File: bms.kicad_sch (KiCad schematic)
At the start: 27 parts, among them J1 I2C+ALERT, Q1 30V/20A_NFET, Q2 30V/20A_NFET, U1 BQ7692003

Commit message: sourcing: lock LCSC + MPN + Manufacturer + Footprint for every remaining BOM line
Applied JLCPCB picks (LCSC number + manufacturer part number + tuned
footprint) across all four sub-sheets — 72 components total.  Every
placed component now carries LCSC, MPN, and Manufacturer properties;
the built-in Value/Footprint fields point to the exact JLCPCB stock
unit for that pick.

Highlights:
- ICs (Preferred where available, Extended otherwise):
    U1(bms)      BQ7692003PWR   C601650    TSSOP-20
    U1(charger)  IP2326         C2832094   VQFN-24 EP4x4
    U1(input)    CH224K         C970725    ESSOP-10
    U1(bckbst)   LM5176PWPR     C442493    HTSSOP-28
- Diodes + TVS (all Preferred tier):
    D1(input)    SRV05-4        C7420376   SOT-23-6   (622K stock)
    D2(input)    SMAJ12A        C19077531  SMA        ( 33K stock)
    D1-3(bms)    SMAJ15A        C19077535  SMA        (174K stock)
- Power passives:
    L1(bckbst)   6.8uH 5A       C167221    FXL0630-6R8-M  7x6.6mm
    L1(charger)  2.2uH 4.8A     C602029    FHD4020S-2R2MT 4x4mm
    FB1(input)   600R@100MHz    C139183    CBW160808U601T 0603 (1A)
    R9(bms)      5mR 2W ±1%     C185817    RLM25FEER005   2512
- Bulk passives — Uniohm 0603WAF series, ±1%, high stock.  All caps
  Samsung/Yageo 0603 or 0805 ceramic.  Reused Q1-Q4 = AON7544
  (already locked at 9120877) for bms.Q1/Q2 too — same part
  covers 30V/20A pack-return FET stack.

Effect on pre-fab readiness (kicad-happy):
- SS-001 error CLEARED — 1/34 MPN coverage was blocking pre-fab;
  now 34/34 (100%).
- DS-002 warning shifted: was "no datasheets" (2/34 MPNs), now
  "no datasheets dir" (34/34 MPNs).  Non-blocking; datasheet PDFs
  are nice-to-have but the review can proceed without them.
- 1 remaining error PP-001 (LM5176_VCC no DC source) is a false
  positive: KiCad library symbol declares VCC as power_in but it's
  actually the LM5176's internal 5V LDO OUTPUT.  Accepted as-is.

Full-project ERC still 0 errors.  Schematic is now sourcing-clean
and ready for 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
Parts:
- BAT1: value 3× 18650 -> BH-18650-B5BA016; LCSC (none) -> C19184086; MPN (none) -> BH-18650-B5BA016; Manufacturer (none) -> MYOUNG
- C1, C2, C3, C4, C6: LCSC (none) -> C14663; MPN (none) -> CC0603KRX7R9BB104; Manufacturer (none) -> YAGEO
- C5, C7: LCSC (none) -> C15849; MPN (none) -> CL10A105KB8NNNC; Manufacturer (none) -> SAMSUNG
- D1, D2, D3: LCSC (none) -> C19077535; MPN (none) -> SMAJ15A; Manufacturer (none) -> LRC
- J1: LCSC (none) -> C492404; MPN (none) -> PZ254V-11-05P; Manufacturer (none) -> XKB Connectivity
- Q1, Q2: value 30V/20A_NFET -> AON7544; footprint Package_TO_SOT_SMD:SOIC-8_3.9x4.9mm_P1.27mm -> power_module_lib:DFN-8_L3.3-W3.3-P0.65-BL-2; LCSC (none) -> C315567; MPN (none) -> AON7544; Manufacturer (none) -> Alpha & Omega Semi
- R1, R10, R11, R2, R3, R4: LCSC (none) -> C22775; MPN (none) -> 0603WAF1000T5E; Manufacturer (none) -> Uniohm
- R5, R6, R7, R8: LCSC (none) -> C25804; MPN (none) -> 0603WAF1002T5E; Manufacturer (none) -> Uniohm
- R9: LCSC (none) -> C185817; MPN (none) -> RLM25FEER005; Manufacturer (none) -> Uniohm
- TH1: LCSC (none) -> C2889048; MPN (none) -> CMFA 103F3435; Manufacturer (none) -> CHIP-TEK
- U1: value BQ7692003 -> BQ7692003PWR; LCSC (none) -> C601650; MPN (none) -> BQ7692003PWR; Manufacturer (none) -> Texas Instruments

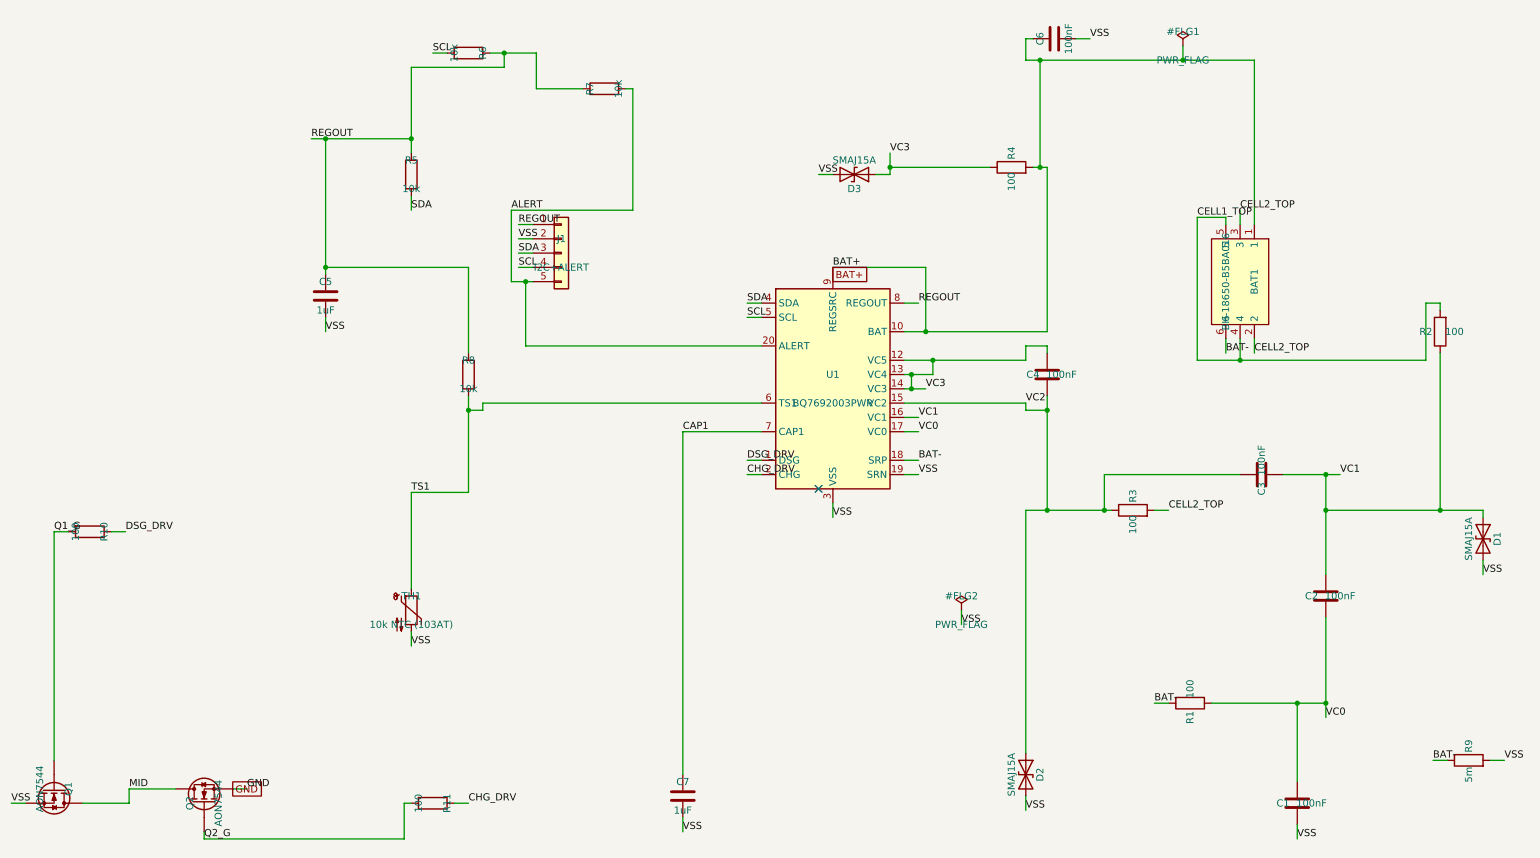
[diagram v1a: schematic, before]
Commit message: sheets: hierarchical ref disambiguation via annotate_schematic
Every sub-sheet symbol now carries a `_{SHEETNAME}{instance_num}` suffix so
refs are globally unique across the hierarchy.  76 refs rewritten:
  bms:       27 (e.g. U1 → U1_BMS1,      Q1 → Q1_BMS1)
  charger:   19 (e.g. U1 → U1_CHARGER1,  R7 → R7_CHARGER1)
  input:      8 (e.g. U1 → U1_INPUT1,    J1 → J1_INPUT1)
  buckboost: 22 (e.g. U1 → U1_BUCKBOOST1,Q1 → Q1_BUCKBOOST1)

Fixes kicad-cli's `schematic has annotation errors` warning which previously
caused BOM export to collapse the four different U1's (BQ76920 + IP2326 +
CH224K + LM5176) into a single row with comma-joined values.

bom_step1.csv committed alongside as the post-disambiguation baseline —
38 grouped rows, 100% LCSC/MPN coverage.

Applied via the new `annotate_schematic` hierarchical pass shipped in
KiCAD-MCP-Server c529efa on develop.  See NOTES.md for the mid-session
handoff block and memory `feedback_hierarchical_annotate`.

Co-Authored-By: Claude Opus 4.7 <noreply@anthropic.com>
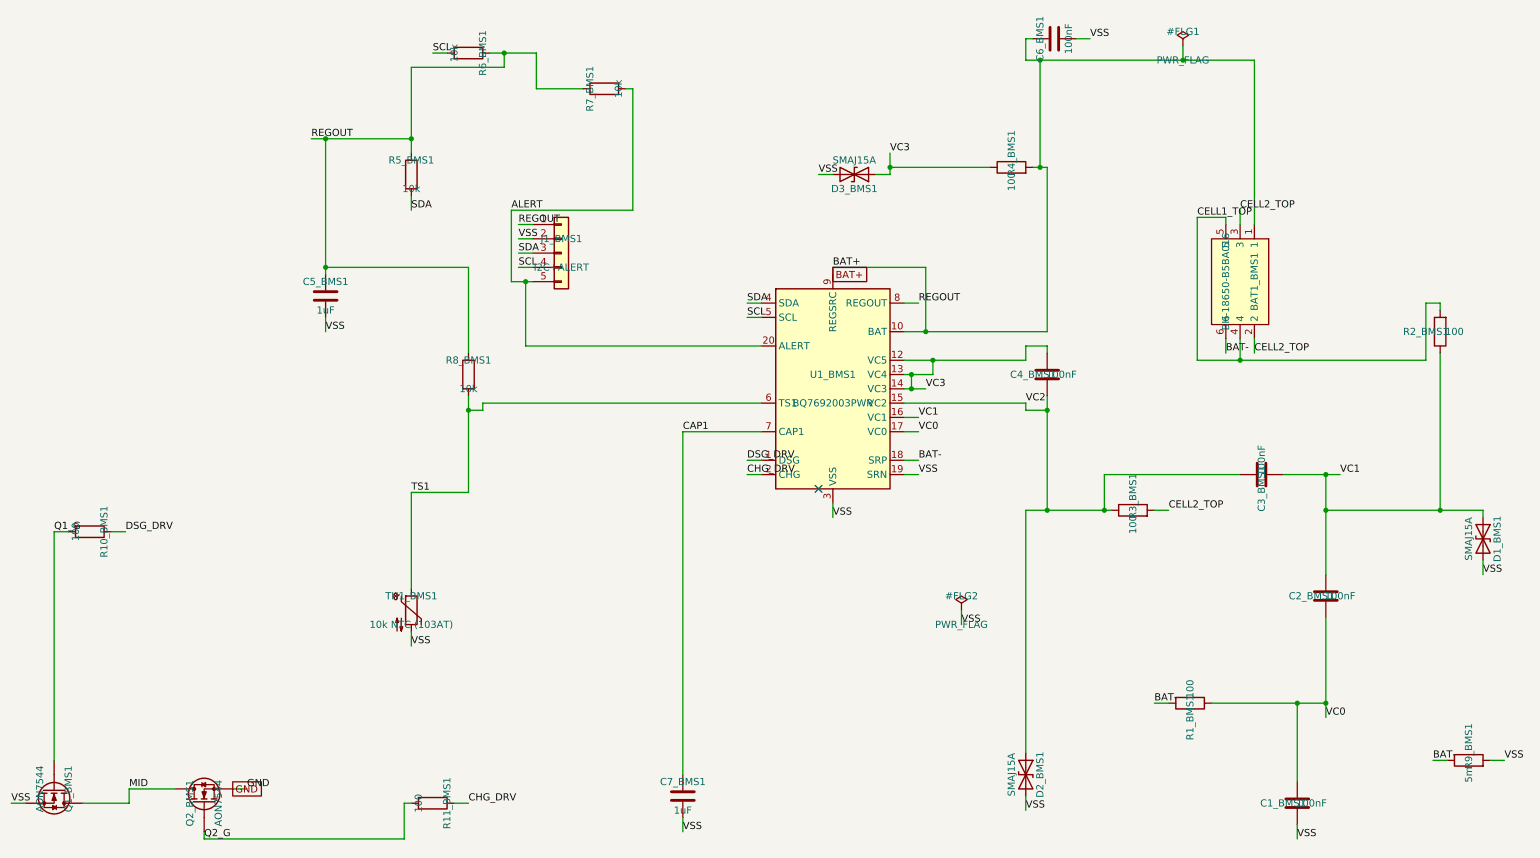
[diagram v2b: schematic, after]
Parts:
- renumbered BAT1 to BAT1_BMS1, C1 to C1_BMS1, C2 to C2_BMS1, C3 to C3_BMS1, C4 to C4_BMS1, C5 to C5_BMS1, C6 to C6_BMS1, C7 to C7_BMS1, D1 to D1_BMS1, D2 to D2_BMS1, D3 to D3_BMS1, J1 to J1_BMS1, Q1 to Q1_BMS1, Q2 to Q2_BMS1, R10 to R10_BMS1, R11 to R11_BMS1, R1 to R1_BMS1, R2 to R2_BMS1, R3 to R3_BMS1, R4 to R4_BMS1, R5 to R5_BMS1, R6 to R6_BMS1, R7 to R7_BMS1, R8 to R8_BMS1, R9 to R9_BMS1, TH1 to TH1_BMS1, U1 to U1_BMS1

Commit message: Step 2: complete Footprint set + sync 76 footprints to .kicad_pcb
Fill in the Footprint properties that were missing from the prior
sourcing pass, and sync everything to the PCB.

Footprint updates on the schematic:
- 35 passives got their Footprint assigned by value (0603 for R/C ≤1uF,
  0805 for 10uF/22uF caps).
- BAT1_BMS1 → power_module_lib:BAT-SMD_BH-18650-B5BA016 (was truncated).
- L1_BUCKBOOST1 → Inductor_SMD:L_Sumida_CDMC6D28_7.25x6.5mm (needed the
  size suffix so KiCad can resolve the .kicad_mod file).

Sync result: 76/76 footprints imported, 60 nets added, 245 pads assigned,
0 import errors.  Unmatched pads reported are all intentional NCs per
REQUIREMENTS.md (USB-C D+/D-, CH224K SBU/CFG, SRV05-4 unused ESD channels).

The footprints are at the default y=-140..-20 auto-import grid; no
placement work yet.  Next step is add_board_outline + set_design_rules.

For discoverability going forward, the pre-sync gap gets caught by
check_sourcing_readiness (KiCAD-MCP-Server fa93ba9 on develop) rather
than having to reset the .kicad_pcb after every retro-fill of an empty
Footprint property.

Co-Authored-By: Claude Opus 4.7 <noreply@anthropic.com>
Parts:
- BAT1_BMS1: footprint (none) -> power_module_lib:BAT-SMD_BH-18650-B5BA016

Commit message: Step 3+4 WIP: board outline, 4-layer stackup, decoupling spring classes, initial placement pass
Step 3 (board mechanics)
- Edge.Cuts rectangle 100x70 mm (BAT1 alone is 82.3x56.8 so 60x80 in
  the pre-session NOTES was too small)
- 4-layer stackup: added In1.Cu (GND plane) + In2.Cu (PWR plane)
- Design rules tightened: clearance 0.15, minTrackWidth 0.15,
  minViaDiameter 0.45, viaDrill 0.3

Step 4 (WIP — placement)
- 13 Pin_Spring_Class:{pad} = {"IC.pin": "DECOUPLING"} assignments on
  bypass caps across bms/charger/buckboost.  Every IC's power/reservoir/
  bootstrap cap now has an explicit DECOUPLING target so the auto-placer
  parks it right next to the IC pin instead of drifting off with the
  power-rail centroid:
    C7_BMS1        -> BQ76920 CAP1 (pin 7, charge pump reservoir)
    C5_BMS1        -> BQ76920 REGOUT bypass (pin 8)
    C6_BMS1        -> BQ76920 BAT+ sense
    C1..C4_BMS1    -> BQ76920 VCn sense RC filters
    C3_BUCKBOOST1  -> LM5176 BIAS bypass (pin 24, 2.2uF)
    C4_BUCKBOOST1  -> LM5176 VCC LDO bypass (pin 23, 1uF)
    C5_BUCKBOOST1  -> LM5176 BOOT1 bootstrap (pin 26)
    C6_BUCKBOOST1  -> LM5176 BOOT2 bootstrap (pin 20)
    C7_BUCKBOOST1  -> LM5176 SS (pin 8)
    C5_CHARGER1    -> IP2326 BST_CAP (pin 14)
- Initial relax_placement pass with 7 locked anchors (2 headers + BAT1 +
  4 ICs).  Not a shippable layout yet: USB-C is backwards, I2C header
  overlaps BAT1's B.Cu pad zone, Q1..Q4 + L1 (buck-boost power stage)
  scattered from LM5176.  Left as a starting point for hand-refinement.
- TH1_BMS1 (pack thermistor) flipped to B.Cu for proximity to the
  cells — final position to be set by hand.

Co-Authored-By: Claude Opus 4.7 <noreply@anthropic.com>
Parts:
- C1_BMS1: Pin_Spring_Class:2 (none) -> {"U1_BMS1.17":"DECOUPLING"}
- C2_BMS1: Pin_Spring_Class:2 (none) -> {"U1_BMS1.16":"DECOUPLING"}
- C3_BMS1: Pin_Spring_Class:2 (none) -> {"U1_BMS1.15":"DECOUPLING"}
- C4_BMS1: Pin_Spring_Class:2 (none) -> {"U1_BMS1.14":"DECOUPLING"}
- C5_BMS1: Pin_Spring_Class:1 (none) -> {"U1_BMS1.8":"DECOUPLING"}
- C6_BMS1: Pin_Spring_Class:1 (none) -> {"U1_BMS1.10":"DECOUPLING"}
- C7_BMS1: Pin_Spring_Class:1 (none) -> {"U1_BMS1.7":"DECOUPLING"}

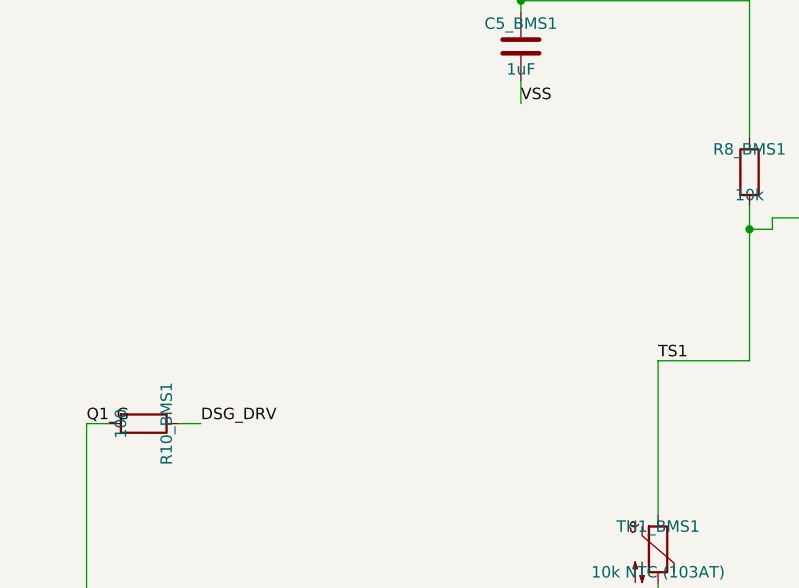
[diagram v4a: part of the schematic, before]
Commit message: Step 4 complete: SW1 kill switch, buck-boost thermal cluster, second relax pass
Kill switch (SW1_BMS1) added to bms sheet.  SPDT slide (Switch:SW_SPDT
symbol, Button_Switch_SMD:SW_SPDT_PCM12 footprint).  Topology:

  BQ76920.DSG_DRV (pin 1)  ──► SW1.1 (throw ON)
                             ▲
  R10_BMS1.1 ── DSG_DRV_GATED ── SW1.2 (common)
                             ▼
                             SW1.3 (throw OFF) ── GND

When switch is in throw 1 (ON) the DSG_DRV signal reaches R10 and drives
Q1's gate normally.  When in throw 3 (OFF) common shorts to GND and pulls
R10.1 low, which via R10 pulls Q1's gate to GND — the discharge FET turns
off and the pack output goes dead.  Charge path (Q2_BMS1) is unaffected,
so the pack can still be charged through the BMS with the switch off.

DSG_DRV split into DSG_DRV (BQ76920 → SW1.1) and DSG_DRV_GATED (SW1.2 →
R10.1).  Sync + `place_component` used because the retroactive-import gap
in sync_schematic_to_board would otherwise leave the SW1 footprint off
the board.

Buck-boost thermal cluster moved to bottom edge

U1_BUCKBOOST1 (LM5176 HTSSOP-28 with EP thermal pad) and the whole
power stage moved out from under BAT1's projected keepout and down to the
bottom-left corner where the board edge acts as a heatsink:

  U1_BUCKBOOST1   → (30, 58)    LM5176
  Q1_BUCKBOOST1   → (18, 55)    buck HS
  Q2_BUCKBOOST1   → (18, 61)    buck LS
  Q3_BUCKBOOST1   → (42, 61)    boost LS
  Q4_BUCKBOOST1   → (42, 55)    boost HS
  L1_BUCKBOOST1   → (30, 66)    SW1↔SW2 inductor
  C1_BUCKBOOST1   → (12, 58)    Cin bulk 22uF
  C2_BUCKBOOST1   → (12, 65)    Cin bulk 22uF
  C10_BUCKBOOST1  → (48, 65)    Cout bulk 22uF
  C11_BUCKBOOST1  → (48, 58)    Cout bulk 22uF

Second relax_placement pass

18 refs locked (2 headers + BAT1 + TH1 + SW1 + 4 ICs + 10 buck-boost).
Everything else pulled toward its natural cluster.  The META1 singleton's
mcp_spring_classes now takes effect: BAT+/VBUS_9V/VBUS_RAW/VOUT_12V/VSYS
are PLANE-classified and no longer distort 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
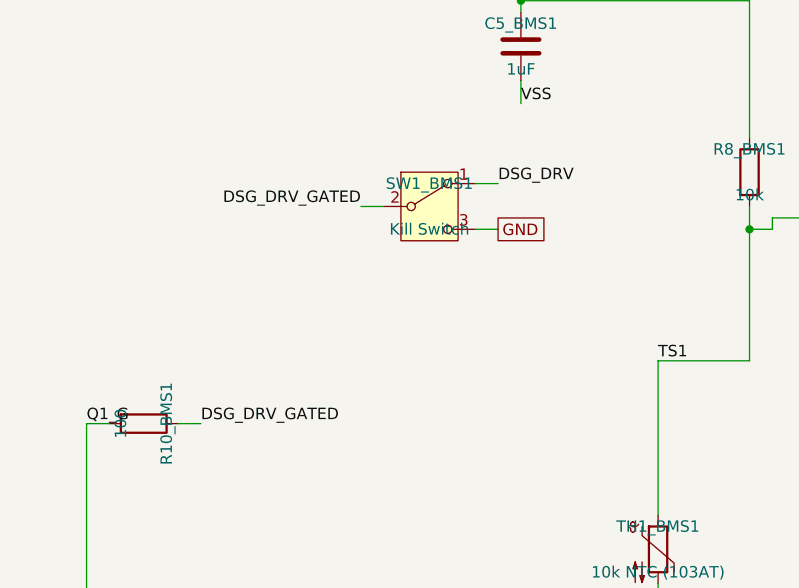
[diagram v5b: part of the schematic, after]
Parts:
- added SW1_BMS1: Kill Switch, Button_Switch_SMD:SW_SPDT_PCM12, symbol Switch:SW_SPDT
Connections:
- net DSG_DRV: now also SW1_BMS1.1 (A); no longer R10_BMS1.1
- net GND: now also SW1_BMS1.3 (C)
- new net DSG_DRV_GATED: R10_BMS1.1, SW1_BMS1.2 (B)

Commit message: R10_BMS1: 100Ω → 1kΩ for Q1 kill-switch turn-off protection
Prior-design failure mode (per user): kill switch shorted Q1's gate
directly to source with NO gate resistor.  A near-zero gate resistance
plus BAT+ trace parasitic inductance meant that when the switch was
thrown mid-discharge, Q1's channel current collapsed in ~10 ns and
the resulting L·(dI/dt) spike drove V_ds far past the AON7544's 30V
avalanche rating — hundreds of volts is easily plausible for ~1 nH of
switch-lead inductance at 5A.

Analysis (see chat log): at R10 = 100Ω, expected V_ds spike from ~1
μH BAT+ parasitic ≈ 14V on top of 12V pack = 26V, on the edge of the
30V spec.  Bumping R10 to 1kΩ slows the gate-side dI/dt by ~5-10×,
dropping the V_ds spike to a few volts and putting the FET well
inside its rated operating envelope.

Downstream impact: turn-on time at boot slows to ~4 μs (τ ≈ 1.2 μs
into Ciss ≈ 1400 pF).  Fine for a battery-protection FET that turns
on once per session.  Turn-off time similarly slows; that's the
point.  No oscillation risk — higher gate resistance damps rather
than induces ringing.

R11_BMS1 (Q2 charge FET gate) left at 100Ω.  The CHG path doesn't
hot-switch under a mechanical kill switch and only turns off/on via
BMS command — a graceful shutdown.

Miller-plateau conduction was also considered (user's original
hypothesis).  Numbers work out to ~8 μJ per turn-off event and
~2.5 mK die temperature rise — thermally invisible.  Overvoltage from
parasitic inductance was the more likely cause of prior failure.

Co-Authored-By: Claude Opus 4.7 <noreply@anthropic.com>
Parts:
- R10_BMS1: value 100 -> 1k; LCSC C22775 -> C21190; MPN 0603WAF1000T5E -> 0603WAF1001T5E; Notes (none) -> Q1 gate turn-off protection; slows dI/dt during kill-switch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
